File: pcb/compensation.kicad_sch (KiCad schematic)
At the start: 12 parts

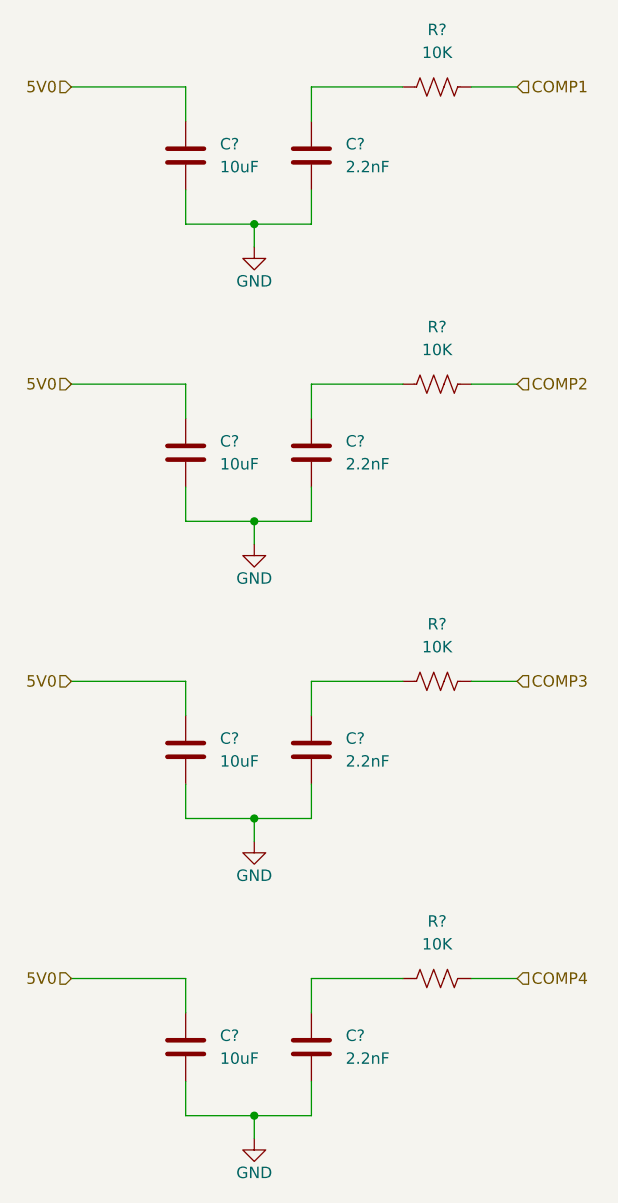
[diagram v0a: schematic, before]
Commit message: changed spi flash to wson
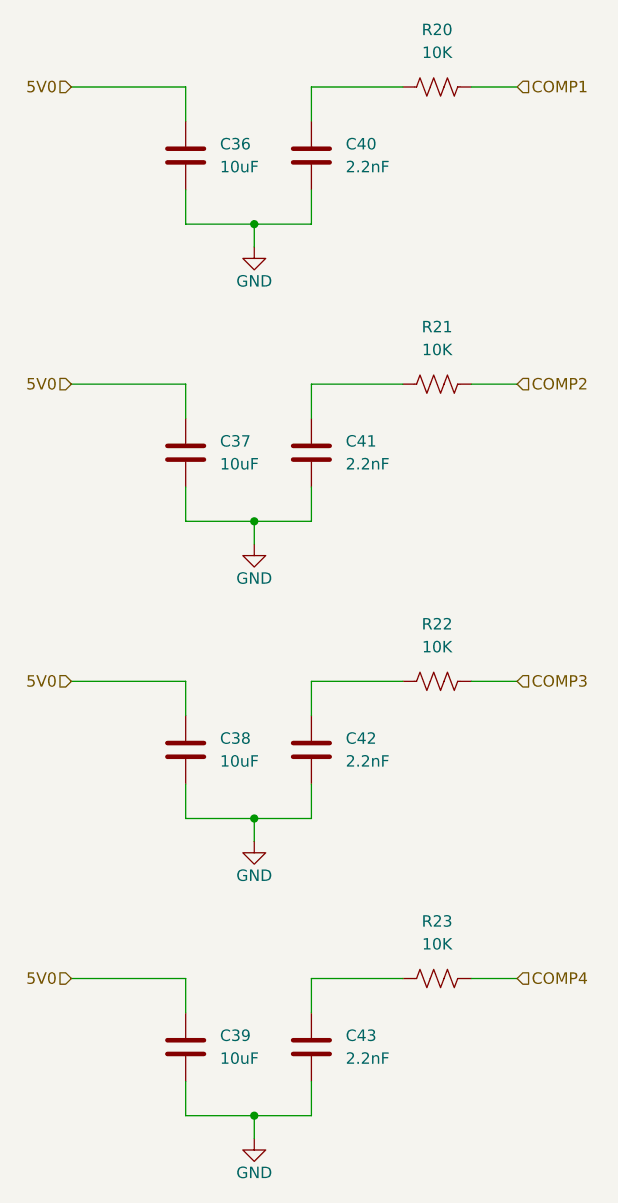
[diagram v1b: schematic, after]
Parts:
- C36, C37, C38, C39: renamed from C?; footprint (none) -> Capacitor_SMD:C_0402_1005Metric
- C40, C41, C42, C43: renamed from C?; footprint (none) -> Capacitor_SMD:C_0201_0603Metric
- R20, R21, R22, R23: renamed from R?; footprint (none) -> Resistor_SMD:R_0402_1005Metric
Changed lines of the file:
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@@
 		(dnp no)
 		(fields_autoplaced yes)
-		(property "Reference" "C?"
+		(property "Reference" "C43"
 			(at 118.11 144.7799 0)
 			(effects
@@
 			)
 		)
-		(property "Footprint" ""
+		(property "Footprint" "Capacitor_SMD:C_0201_0603Metric"
 			(at 115.2652 149.86 0)
 			(effects
@@
 			(project "RPi-HwAB-1"
 				(path "/e63e39d7-6ac0-4ffd-8aa3-1841a4541b55/f9ebb56c-78c7-42ac-bc19-ccbf788f5318/dc89b573-6958-4e1d-ba95-c35e0bbf4438"
-					(reference "C?")
+					(reference "C43")
 					(unit 1)
 				)
@@
 		(dnp no)
 		(fields_autoplaced yes)
-		(property "Reference" "C?"
+		(property "Reference" "C42"
 			(at 118.11 111.7599 0)
 			(effects
@@
 			)
 		)
-		(property "Footprint" ""
+		(property "Footprint" "Capacitor_SMD:C_0201_0603Metric"
 			(at 115.2652 116.84 0)
 			(effects
@@
 			(project "RPi-HwAB-1"
 				(path "/e63e39d7-6ac0-4ffd-8aa3-1841a4541b55/f9ebb56c-78c7-42ac-bc19-ccbf788f5318/dc89b573-6958-4e1d-ba95-c35e0bbf4438"
-					(reference "C?")
+					(reference "C42")
 					(unit 1)
 				)
@@
 		(dnp no)
 		(fields_autoplaced yes)
-		(property "Reference" "C?"
+		(property "Reference" "C39"
 			(at 104.14 144.7799 0)
 			(effects
@@
 			)
 		)
-		(property "Footprint" ""
+		(property "Footprint" "Capacitor_SMD:C_0402_1005Metric"
 			(at 101.2952 149.86 0)
 			(effects
@@
 			(project "RPi-HwAB-1"
 				(path "/e63e39d7-6ac0-4ffd-8aa3-1841a4541b55/f9ebb56c-78c7-42ac-bc19-ccbf788f5318/dc89b573-6958-4e1d-ba95-c35e0bbf4438"
-					(reference "C?")
+					(reference "C39")
 					(unit 1)
 				)
@@
 		(dnp no)
 		(fields_autoplaced yes)
-		(property "Reference" "C?"
+		(property "Reference" "C40"
 			(at 118.11 45.7199 0)
 			(effects
@@
 			)
 		)
-		(property "Footprint" ""
+		(property "Footprint" "Capacitor_SMD:C_0201_0603Metric"
 			(at 115.2652 50.8 0)
 			(effects
@@
 			(project "RPi-HwAB-1"
 				(path "/e63e39d7-6ac0-4ffd-8aa3-1841a4541b55/f9ebb56c-78c7-42ac-bc19-ccbf788f5318/dc89b573-6958-4e1d-ba95-c35e0bbf4438"
-					(reference "C?")
+					(reference "C40")
 					(unit 1)
 				)
@@
 		(dnp no)
 		(fields_autoplaced yes)
-		(property "Reference" "R?"
+		(property "Reference" "R22"
 			(at 128.27 99.06 90)
 			(effects
@@
 			)
 		)
-		(property "Footprint" ""
+		(property "Footprint" "Resistor_SMD:R_0402_1005Metric"
 			(at 128.524 104.394 90)
 			(effects
@@
 			(project "RPi-HwAB-1"
 				(path "/e63e39d7-6ac0-4ffd-8aa3-1841a4541b55/f9ebb56c-78c7-42ac-bc19-ccbf788f5318/dc89b573-6958-4e1d-ba95-c35e0bbf4438"
-					(reference "R?")
+					(reference "R22")
 					(unit 1)
 				)
@@
 		(dnp no)
 		(fields_autoplaced yes)
-		(property "Reference" "R?"
+		(property "Reference" "R21"
 			(at 128.27 66.04 90)
 			(effects
@@
 			)
 		)
-		(property "Footprint" ""
+		(property "Footprint" "Resistor_SMD:R_0402_1005Metric"
 			(at 128.524 71.374 90)
 			(effects
@@
 			(project "RPi-HwAB-1"
 				(path "/e63e39d7-6ac0-4ffd-8aa3-1841a4541b55/f9ebb56c-78c7-42ac-bc19-ccbf788f5318/dc89b573-6958-4e1d-ba95-c35e0bbf4438"
-					(reference "R?")
+					(reference "R21")
 					(unit 1)
 				)
@@
 		(dnp no)
 		(fields_autoplaced yes)
-		(property "Reference" "R?"
+		(property "Reference" "R20"
 			(at 128.27 33.02 90)
 			(effects
@@
 			)
 		)
-		(property "Footprint" ""
+		(property "Footprint" "Resistor_SMD:R_0402_1005Metric"
 			(at 128.524 38.354 90)
 			(effects
@@
 			(project "RPi-HwAB-1"
 				(path "/e63e39d7-6ac0-4ffd-8aa3-1841a4541b55/f9ebb56c-78c7-42ac-bc19-ccbf788f5318/dc89b573-6958-4e1d-ba95-c35e0bbf4438"
-					(reference "R?")
+					(reference "R20")
 					(unit 1)
 				)
@@
 		(dnp no)
 		(fields_autoplaced yes)
-		(property "Reference" "C?"
+		(property "Reference" "C37"
 			(at 104.14 78.7399 0)
 			(effects
@@
 			)
 		)
-		(property "Footprint" ""
+		(property "Footprint" "Capacitor_SMD:C_0402_1005Metric"
 			(at 101.2952 83.82 0)
 			(effects
@@
 			(project "RPi-HwAB-1"
 				(path "/e63e39d7-6ac0-4ffd-8aa3-1841a4541b55/f9ebb56c-78c7-42ac-bc19-ccbf788f5318/dc89b573-6958-4e1d-ba95-c35e0bbf4438"
-					(reference "C?")
+					(reference "C37")
 					(unit 1)
 				)
@@
 		(dnp no)
 		(fields_autoplaced yes)
-		(property "Reference" "C?"
+		(property "Reference" "C41"
 			(at 118.11 78.7399 0)
 			(effects
@@
 			)
 		)
-		(property "Footprint" ""
+		(property "Footprint" "Capacitor_SMD:C_0201_0603Metric"
 			(at 115.2652 83.82 0)
 			(effects
@@
 			(project "RPi-HwAB-1"
 				(path "/e63e39d7-6ac0-4ffd-8aa3-1841a4541b55/f9ebb56c-78c7-42ac-bc19-ccbf788f5318/dc89b573-6958-4e1d-ba95-c35e0bbf4438"
-					(reference "C?")
+					(reference "C41")
 					(unit 1)
 				)
@@
 		(dnp no)
 		(fields_autoplaced yes)
-		(property "Reference" "R?"
+		(property "Reference" "R23"
 			(at 128.27 132.08 90)
 			(effects
@@
 			)
 		)
-		(property "Footprint" ""
+		(property "Footprint" "Resistor_SMD:R_0402_1005Metric"
 			(at 128.524 137.414 90)
 			(effects
@@
 			(project "RPi-HwAB-1"
 				(path "/e63e39d7-6ac0-4ffd-8aa3-1841a4541b55/f9ebb56c-78c7-42ac-bc19-ccbf788f5318/dc89b573-6958-4e1d-ba95-c35e0bbf4438"
-					(reference "R?")
+					(reference "R23")
 					(unit 1)
 				)
@@
 		(dnp no)
 		(fields_autoplaced yes)
-		(property "Reference" "C?"
+		(property "Reference" "C38"
 			(at 104.14 111.7599 0)
 			(effects
@@
 			)
 		)
-		(property "Footprint" ""
+		(property "Footprint" "Capacitor_SMD:C_0402_1005Metric"
 			(at 101.2952 116.84 0)
 			(effects
@@
 			(project "RPi-HwAB-1"
 				(path "/e63e39d7-6ac0-4ffd-8aa3-1841a4541b55/f9ebb56c-78c7-42ac-bc19-ccbf788f5318/dc89b573-6958-4e1d-ba95-c35e0bbf4438"
-					(reference "C?")
+					(reference "C38")
 					(unit 1)
 				)
@@
 		(dnp no)
 		(fields_autoplaced yes)
-		(property "Reference" "C?"
+		(property "Reference" "C36"
 			(at 104.14 45.7199 0)
 			(effects
@@
 			)
 		)
-		(property "Footprint" ""
+		(property "Footprint" "Capacitor_SMD:C_0402_1005Metric"
 			(at 101.2952 50.8 0)
 			(effects
@@
 			(project "RPi-HwAB-1"
 				(path "/e63e39d7-6ac0-4ffd-8aa3-1841a4541b55/f9ebb56c-78c7-42ac-bc19-ccbf788f5318/dc89b573-6958-4e1d-ba95-c35e0bbf4438"
-					(reference "C?")
-					(unit 1)
-				)
+					(reference "C36")
+					(unit 1)
+				)

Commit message: saved libraries to project
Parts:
- C36, C37, C38, C39, C40, C41, C42, C43: symbol Device:C -> library:C
- R20, R21, R22, R23: symbol Device:R_US -> library:R_US
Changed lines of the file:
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@@
 	)
 	(symbol
-		(lib_id "Device:C")
+		(lib_id "library:C")
 		(at 114.3 146.05 0)
 		(unit 1)
@@
 	)
 	(symbol
-		(lib_id "Device:C")
+		(lib_id "library:C")
 		(at 114.3 113.03 0)
 		(unit 1)
@@
 	)
 	(symbol
-		(lib_id "Device:C")
+		(lib_id "library:C")
 		(at 100.33 146.05 0)
 		(unit 1)
@@
 	)
 	(symbol
-		(lib_id "Device:C")
+		(lib_id "library:C")
 		(at 114.3 46.99 0)
 		(unit 1)
@@
 	)
 	(symbol
-		(lib_id "Device:R_US")
+		(lib_id "library:R_US")
 		(at 128.27 105.41 90)
 		(unit 1)
@@
 	)
 	(symbol
-		(lib_id "power:GND")
+		(lib_id "library:GND")
 		(at 107.95 123.19 0)
 		(unit 1)
@@
 	)
 	(symbol
-		(lib_id "Device:R_US")
+		(lib_id "library:R_US")
 		(at 128.27 72.39 90)
 		(unit 1)
@@
 	)
 	(symbol
-		(lib_id "Device:R_US")
+		(lib_id "library:R_US")
 		(at 128.27 39.37 90)
 		(unit 1)
@@
 	)
 	(symbol
-		(lib_id "Device:C")
+		(lib_id "library:C")
 		(at 100.33 80.01 0)
 		(unit 1)
@@
 	)
 	(symbol
-		(lib_id "power:GND")
+		(lib_id "library:GND")
 		(at 107.95 90.17 0)
 		(unit 1)
@@
 	)
 	(symbol
-		(lib_id "Device:C")
+		(lib_id "library:C")
 		(at 114.3 80.01 0)
 		(unit 1)
@@
 	)
 	(symbol
-		(lib_id "Device:R_US")
+		(lib_id "library:R_US")
 		(at 128.27 138.43 90)
 		(unit 1)
@@
 	)
 	(symbol
-		(lib_id "power:GND")
+		(lib_id "library:GND")
 		(at 107.95 57.15 0)
 		(unit 1)
@@
 	)
 	(symbol
-		(lib_id "Device:C")
+		(lib_id "library:C")
 		(at 100.33 113.03 0)
 		(unit 1)
@@
 	)
 	(symbol
-		(lib_id "Device:C")
+		(lib_id "library:C")
 		(at 100.33 46.99 0)
 		(unit 1)
@@
 	)
 	(symbol
-		(lib_id "power:GND")
+		(lib_id "library:GND")
 		(at 107.95 156.21 0)
 		(unit 1)

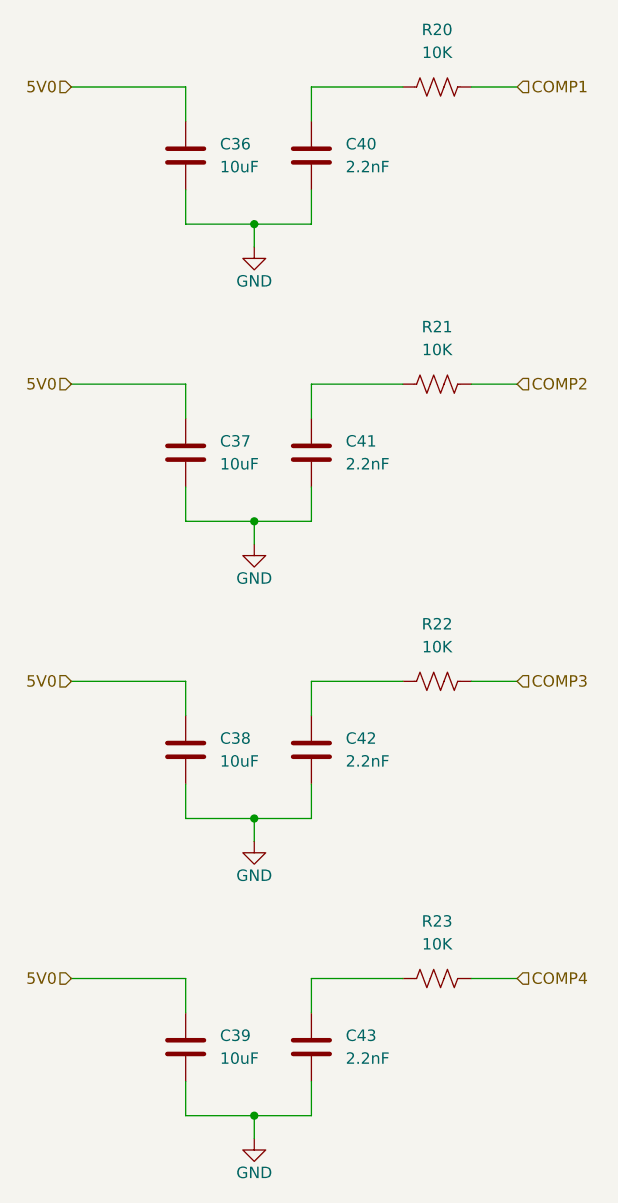
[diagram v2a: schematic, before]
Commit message: defined memory pinouts
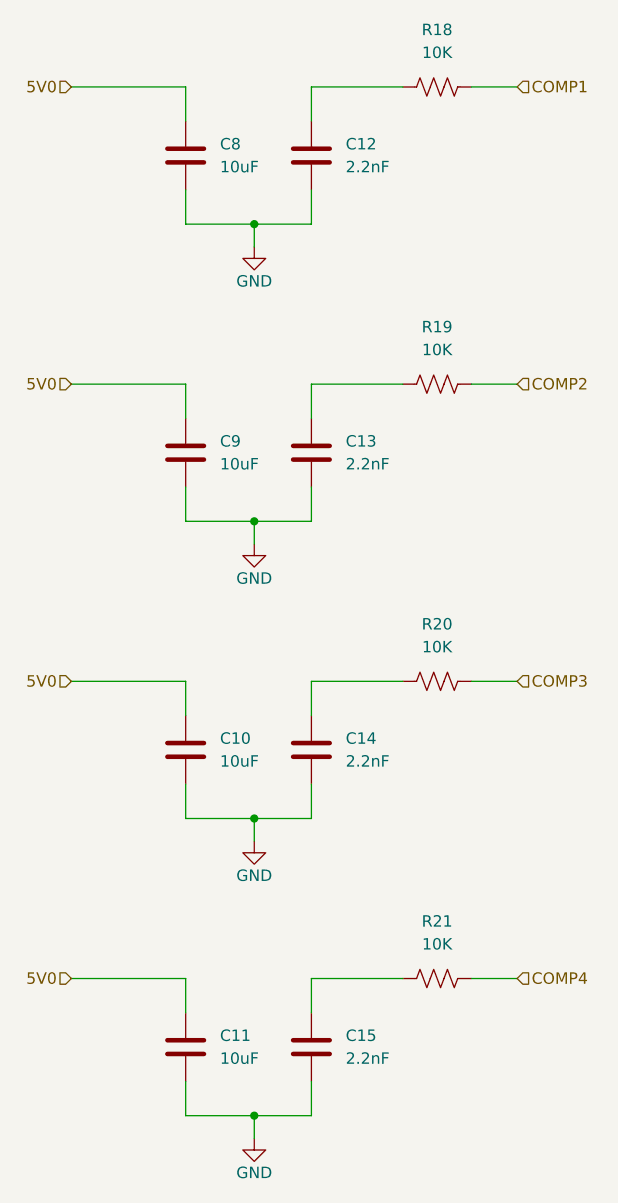
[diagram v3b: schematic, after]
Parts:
- renumbered C38 to C10, C39 to C11, C40 to C12, C41 to C13, C42 to C14, C43 to C15, C36 to C8, C37 to C9, R20 to R18, R21 to R19, R22 to R20, R23 to R21
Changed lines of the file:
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@@
 		(dnp no)
 		(fields_autoplaced yes)
-		(property "Reference" "C43"
+		(property "Reference" "C15"
 			(at 118.11 144.7799 0)
 			(effects
@@
 			(project "RPi-HwAB-1"
 				(path "/e63e39d7-6ac0-4ffd-8aa3-1841a4541b55/f9ebb56c-78c7-42ac-bc19-ccbf788f5318/dc89b573-6958-4e1d-ba95-c35e0bbf4438"
-					(reference "C43")
+					(reference "C15")
 					(unit 1)
 				)
@@
 		(dnp no)
 		(fields_autoplaced yes)
-		(property "Reference" "C42"
+		(property "Reference" "C14"
 			(at 118.11 111.7599 0)
 			(effects
@@
 			(project "RPi-HwAB-1"
 				(path "/e63e39d7-6ac0-4ffd-8aa3-1841a4541b55/f9ebb56c-78c7-42ac-bc19-ccbf788f5318/dc89b573-6958-4e1d-ba95-c35e0bbf4438"
-					(reference "C42")
+					(reference "C14")
 					(unit 1)
 				)
@@
 		(dnp no)
 		(fields_autoplaced yes)
-		(property "Reference" "C39"
+		(property "Reference" "C11"
 			(at 104.14 144.7799 0)
 			(effects
@@
 			(project "RPi-HwAB-1"
 				(path "/e63e39d7-6ac0-4ffd-8aa3-1841a4541b55/f9ebb56c-78c7-42ac-bc19-ccbf788f5318/dc89b573-6958-4e1d-ba95-c35e0bbf4438"
-					(reference "C39")
+					(reference "C11")
 					(unit 1)
 				)
@@
 		(dnp no)
 		(fields_autoplaced yes)
-		(property "Reference" "C40"
+		(property "Reference" "C12"
 			(at 118.11 45.7199 0)
 			(effects
@@
 			(project "RPi-HwAB-1"
 				(path "/e63e39d7-6ac0-4ffd-8aa3-1841a4541b55/f9ebb56c-78c7-42ac-bc19-ccbf788f5318/dc89b573-6958-4e1d-ba95-c35e0bbf4438"
-					(reference "C40")
+					(reference "C12")
 					(unit 1)
 				)
@@
 		(dnp no)
 		(fields_autoplaced yes)
-		(property "Reference" "R22"
+		(property "Reference" "R20"
 			(at 128.27 99.06 90)
 			(effects
@@
 			(project "RPi-HwAB-1"
 				(path "/e63e39d7-6ac0-4ffd-8aa3-1841a4541b55/f9ebb56c-78c7-42ac-bc19-ccbf788f5318/dc89b573-6958-4e1d-ba95-c35e0bbf4438"
-					(reference "R22")
+					(reference "R20")
 					(unit 1)
 				)
@@
 		(on_board yes)
 		(dnp no)
-		(property "Reference" "#PWR024"
+		(property "Reference" "#PWR012"
 			(at 107.95 129.54 0)
 			(effects
@@
 			(project "RPi-HwAB-1"
 				(path "/e63e39d7-6ac0-4ffd-8aa3-1841a4541b55/f9ebb56c-78c7-42ac-bc19-ccbf788f5318/dc89b573-6958-4e1d-ba95-c35e0bbf4438"
-					(reference "#PWR024")
+					(reference "#PWR012")
 					(unit 1)
 				)
@@
 		(dnp no)
 		(fields_autoplaced yes)
-		(property "Reference" "R21"
+		(property "Reference" "R19"
 			(at 128.27 66.04 90)
 			(effects
@@
 			(project "RPi-HwAB-1"
 				(path "/e63e39d7-6ac0-4ffd-8aa3-1841a4541b55/f9ebb56c-78c7-42ac-bc19-ccbf788f5318/dc89b573-6958-4e1d-ba95-c35e0bbf4438"
-					(reference "R21")
+					(reference "R19")
 					(unit 1)
 				)
@@
 		(dnp no)
 		(fields_autoplaced yes)
-		(property "Reference" "R20"
+		(property "Reference" "R18"
 			(at 128.27 33.02 90)
 			(effects
@@
 			(project "RPi-HwAB-1"
 				(path "/e63e39d7-6ac0-4ffd-8aa3-1841a4541b55/f9ebb56c-78c7-42ac-bc19-ccbf788f5318/dc89b573-6958-4e1d-ba95-c35e0bbf4438"
-					(reference "R20")
+					(reference "R18")
 					(unit 1)
 				)
@@
 		(dnp no)
 		(fields_autoplaced yes)
-		(property "Reference" "C37"
+		(property "Reference" "C9"
 			(at 104.14 78.7399 0)
 			(effects
@@
 			(project "RPi-HwAB-1"
 				(path "/e63e39d7-6ac0-4ffd-8aa3-1841a4541b55/f9ebb56c-78c7-42ac-bc19-ccbf788f5318/dc89b573-6958-4e1d-ba95-c35e0bbf4438"
-					(reference "C37")
+					(reference "C9")
 					(unit 1)
 				)
@@
 		(on_board yes)
 		(dnp no)
-		(property "Reference" "#PWR023"
+		(property "Reference" "#PWR011"
 			(at 107.95 96.52 0)
 			(effects
@@
 			(project "RPi-HwAB-1"
 				(path "/e63e39d7-6ac0-4ffd-8aa3-1841a4541b55/f9ebb56c-78c7-42ac-bc19-ccbf788f5318/dc89b573-6958-4e1d-ba95-c35e0bbf4438"
-					(reference "#PWR023")
+					(reference "#PWR011")
 					(unit 1)
 				)
@@
 		(dnp no)
 		(fields_autoplaced yes)
-		(property "Reference" "C41"
+		(property "Reference" "C13"
 			(at 118.11 78.7399 0)
 			(effects
@@
 			(project "RPi-HwAB-1"
 				(path "/e63e39d7-6ac0-4ffd-8aa3-1841a4541b55/f9ebb56c-78c7-42ac-bc19-ccbf788f5318/dc89b573-6958-4e1d-ba95-c35e0bbf4438"
-					(reference "C41")
+					(reference "C13")
 					(unit 1)
 				)
@@
 		(dnp no)
 		(fields_autoplaced yes)
-		(property "Reference" "R23"
+		(property "Reference" "R21"
 			(at 128.27 132.08 90)
 			(effects
@@
 			(project "RPi-HwAB-1"
 				(path "/e63e39d7-6ac0-4ffd-8aa3-1841a4541b55/f9ebb56c-78c7-42ac-bc19-ccbf788f5318/dc89b573-6958-4e1d-ba95-c35e0bbf4438"
-					(reference "R23")
+					(reference "R21")
 					(unit 1)
 				)
@@
 		(on_board yes)
 		(dnp no)
-		(property "Reference" "#PWR022"
+		(property "Reference" "#PWR010"
 			(at 107.95 63.5 0)
 			(effects
@@
 			(project "RPi-HwAB-1"
 				(path "/e63e39d7-6ac0-4ffd-8aa3-1841a4541b55/f9ebb56c-78c7-42ac-bc19-ccbf788f5318/dc89b573-6958-4e1d-ba95-c35e0bbf4438"
-					(reference "#PWR022")
+					(reference "#PWR010")
 					(unit 1)
 				)
@@
 		(dnp no)
 		(fields_autoplaced yes)
-		(property "Reference" "C38"
+		(property "Reference" "C10"
 			(at 104.14 111.7599 0)
 			(effects
@@
 			(project "RPi-HwAB-1"
 				(path "/e63e39d7-6ac0-4ffd-8aa3-1841a4541b55/f9ebb56c-78c7-42ac-bc19-ccbf788f5318/dc89b573-6958-4e1d-ba95-c35e0bbf4438"
-					(reference "C38")
+					(reference "C10")
 					(unit 1)
 				)
@@
 		(dnp no)
 		(fields_autoplaced yes)
-		(property "Reference" "C36"
+		(property "Reference" "C8"
 			(at 104.14 45.7199 0)
 			(effects
@@
 			(project "RPi-HwAB-1"
 				(path "/e63e39d7-6ac0-4ffd-8aa3-1841a4541b55/f9ebb56c-78c7-42ac-bc19-ccbf788f5318/dc89b573-6958-4e1d-ba95-c35e0bbf4438"
-					(reference "C36")
+					(reference "C8")
 					(unit 1)
 				)
@@
 		(on_board yes)
 		(dnp no)
-		(property "Reference" "#PWR025"
+		(property "Reference" "#PWR013"
 			(at 107.95 162.56 0)
 			(effects
@@
 			(project "RPi-HwAB-1"
 				(path "/e63e39d7-6ac0-4ffd-8aa3-1841a4541b55/f9ebb56c-78c7-42ac-bc19-ccbf788f5318/dc89b573-6958-4e1d-ba95-c35e0bbf4438"
-					(reference "#PWR025")
-					(unit 1)
-				)
+					(reference "#PWR013")
+					(unit 1)
+				)
